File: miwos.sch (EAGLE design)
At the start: 44 parts, among them J1 614004190021, U1 PEC16, U3 PEC16

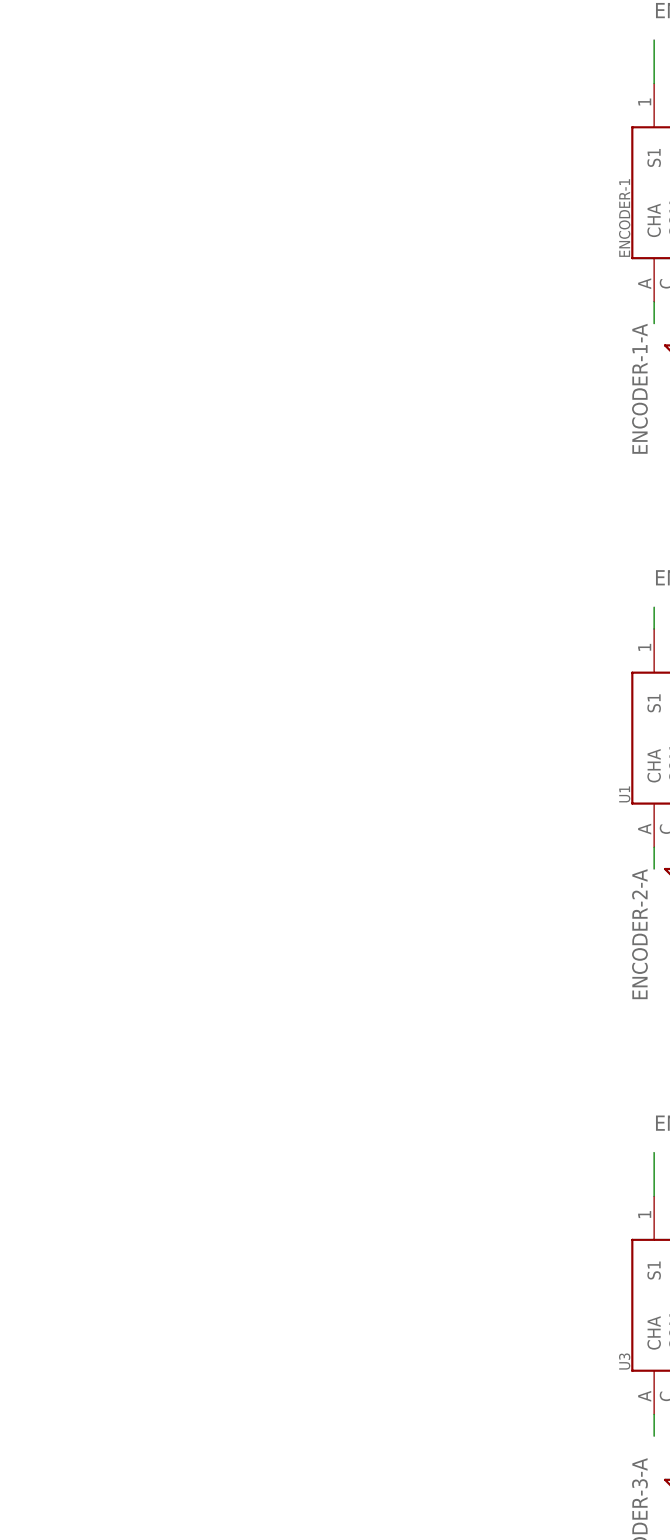
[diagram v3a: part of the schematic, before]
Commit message: Add encoder LEDs, don't wire them for now
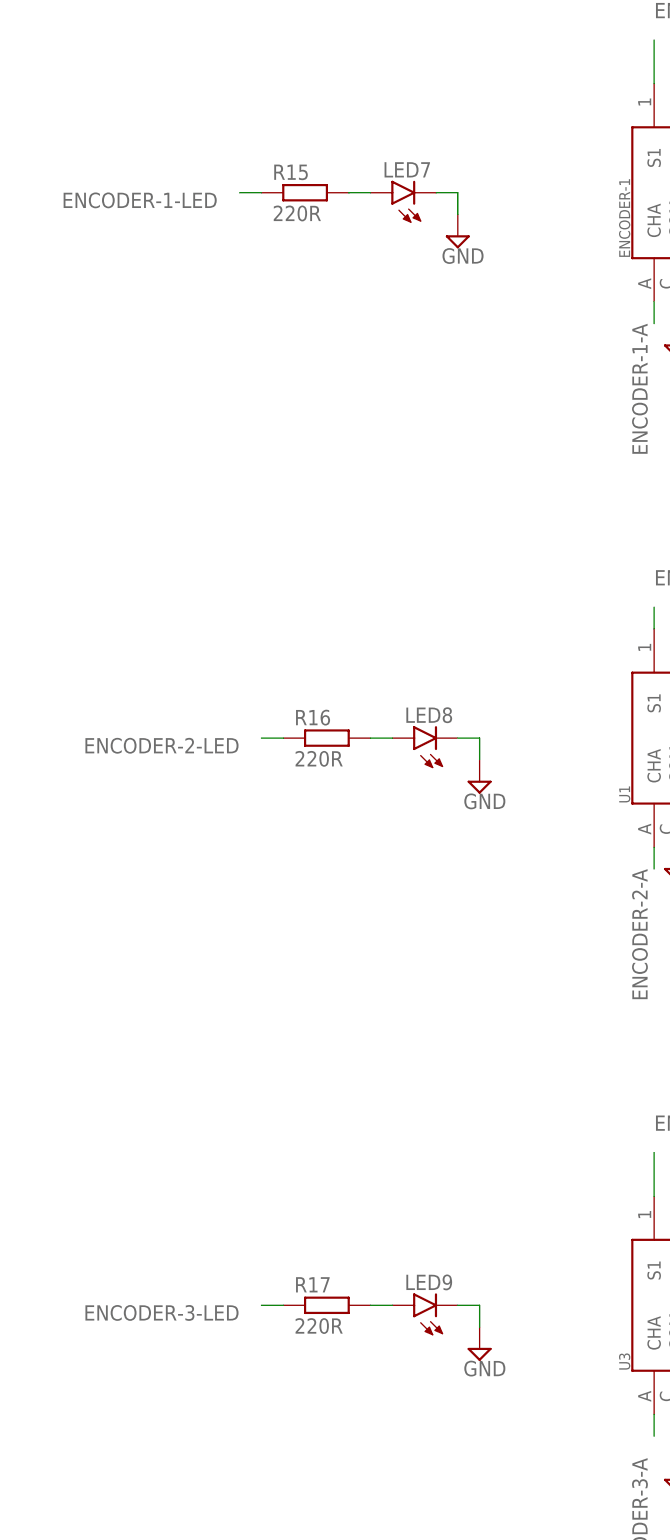
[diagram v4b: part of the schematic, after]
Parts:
- added LED7, LED8, LED9: (no value), led:LED3MM
- added R15, R16, R17: 220R, rcl:R-EU_R0603
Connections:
- new net ENCODER-1-LED: R15.1
- new net ENCODER-2-LED: R16.1
- new net ENCODER-3-LED: R17.1
- new net N$20: LED8.A, R16.2
- new net N$22: LED9.A, R17.2
- new net N$4: LED7.A, R15.2
- net GND: now also LED7.C, LED8.C, LED9.C
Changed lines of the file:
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@@
 <part name="P+4" library="supply1" library_urn="urn:adsk.eagle:library:371" deviceset="+5V" device=""/>
 <part name="SUPPLY29" library="supply2" library_urn="urn:adsk.eagle:library:372" deviceset="GND" device=""/>
+<part name="LED7" library="led" library_urn="urn:adsk.eagle:library:259" deviceset="LED" device="3MM" package3d_urn="urn:adsk.eagle:package:15797/1"/>
+<part name="SUPPLY30" library="supply2" library_urn="urn:adsk.eagle:library:372" deviceset="GND" device=""/>
+<part name="R15" library="rcl" library_urn="urn:adsk.eagle:library:334" deviceset="R-EU_" device="R0603" package3d_urn="urn:adsk.eagle:package:23555/3" value="220R"/>
+<part name="LED8" library="led" library_urn="urn:adsk.eagle:library:259" deviceset="LED" device="3MM" package3d_urn="urn:adsk.eagle:package:15797/1"/>
+<part name="SUPPLY31" library="supply2" library_urn="urn:adsk.eagle:library:372" deviceset="GND" device=""/>
+<part name="R16" library="rcl" library_urn="urn:adsk.eagle:library:334" deviceset="R-EU_" device="R0603" package3d_urn="urn:adsk.eagle:package:23555/3" value="220R"/>
+<part name="LED9" library="led" library_urn="urn:adsk.eagle:library:259" deviceset="LED" device="3MM" package3d_urn="urn:adsk.eagle:package:15797/1"/>
+<part name="SUPPLY32" library="supply2" library_urn="urn:adsk.eagle:library:372" deviceset="GND" device=""/>
+<part name="R17" library="rcl" library_urn="urn:adsk.eagle:library:334" deviceset="R-EU_" device="R0603" package3d_urn="urn:adsk.eagle:package:23555/3" value="220R"/>
 </parts>
 <sheets>
@@
 <instance part="SUPPLY29" gate="GND" x="93.98" y="-5.08" smashed="yes">
 <attribute name="VALUE" x="92.075" y="-8.255" size="1.778" layer="96"/>
+</instance>
+<instance part="LED7" gate="G$1" x="-116.84" y="119.38" smashed="yes" rot="R90">
+<attribute name="NAME" x="-112.268" y="122.936" size="1.778" layer="95" rot="R180"/>
+<attribute name="VALUE" x="-112.268" y="125.095" size="1.778" layer="96" rot="R180"/>
+</instance>
+<instance part="SUPPLY30" gate="GND" x="-109.22" y="114.3" smashed="yes">
+<attribute name="VALUE" x="-111.125" y="111.125" size="1.778" layer="96"/>
+</instance>
+<instance part="R15" gate="G$1" x="-127" y="119.38" smashed="yes">
+<attribute name="NAME" x="-130.81" y="120.8786" size="1.778" layer="95"/>
+<attribute name="VALUE" x="-130.81" y="116.078" size="1.778" layer="96"/>
+</instance>
+<instance part="LED8" gate="G$1" x="-114.3" y="55.88" smashed="yes" rot="R90">
+<attribute name="NAME" x="-109.728" y="59.436" size="1.778" layer="95" rot="R180"/>
+<attribute name="VALUE" x="-109.728" y="61.595" size="1.778" layer="96" rot="R180"/>
+</instance>
+<instance part="SUPPLY31" gate="GND" x="-106.68" y="50.8" smashed="yes">
+<attribute name="VALUE" x="-108.585" y="47.625" size="1.778" layer="96"/>
+</instance>
+<instance part="R16" gate="G$1" x="-124.46" y="55.88" smashed="yes">
+<attribute name="NAME" x="-128.27" y="57.3786" size="1.778" layer="95"/>
+<attribute name="VALUE" x="-128.27" y="52.578" size="1.778" layer="96"/>
+</instance>
+<instance part="LED9" gate="G$1" x="-114.3" y="-10.16" smashed="yes" rot="R90">
+<attribute name="NAME" x="-109.728" y="-6.604" size="1.778" layer="95" rot="R180"/>
+<attribute name="VALUE" x="-109.728" y="-4.445" size="1.778" layer="96" rot="R180"/>
+</instance>
+<instance part="SUPPLY32" gate="GND" x="-106.68" y="-15.24" smashed="yes">
+<attribute name="VALUE" x="-108.585" y="-18.415" size="1.778" layer="96"/>
+</instance>
+<instance part="R17" gate="G$1" x="-124.46" y="-10.16" smashed="yes">
+<attribute name="NAME" x="-128.27" y="-8.6614" size="1.778" layer="95"/>
+<attribute name="VALUE" x="-128.27" y="-13.462" size="1.778" layer="96"/>
 </instance>
 </instances>
@@
 <pinref part="SUPPLY29" gate="GND" pin="GND"/>
 </segment>
+<segment>
+<pinref part="LED7" gate="G$1" pin="C"/>
+<pinref part="SUPPLY30" gate="GND" pin="GND"/>
+<wire x1="-111.76" y1="119.38" x2="-109.22" y2="119.38" width="0.1524" layer="91"/>
+<wire x1="-109.22" y1="119.38" x2="-109.22" y2="116.84" width="0.1524" layer="91"/>
+</segment>
+<segment>
+<pinref part="LED8" gate="G$1" pin="C"/>
+<pinref part="SUPPLY31" gate="GND" pin="GND"/>
+<wire x1="-109.22" y1="55.88" x2="-106.68" y2="55.88" width="0.1524" layer="91"/>
+<wire x1="-106.68" y1="55.88" x2="-106.68" y2="53.34" width="0.1524" layer="91"/>
+</segment>
+<segment>
+<pinref part="LED9" gate="G$1" pin="C"/>
+<pinref part="SUPPLY32" gate="GND" pin="GND"/>
+<wire x1="-109.22" y1="-10.16" x2="-106.68" y2="-10.16" width="0.1524" layer="91"/>
+<wire x1="-106.68" y1="-10.16" x2="-106.68" y2="-12.7" width="0.1524" layer="91"/>
+</segment>
 </net>
 <net name="ENCODER-2-A" class="0">
@@
 </segment>
 </net>
+<net name="N$4" class="0">
+<segment>
+<pinref part="LED7" gate="G$1" pin="A"/>
+<wire x1="-119.38" y1="119.38" x2="-121.92" y2="119.38" width="0.1524" layer="91"/>
+<pinref part="R15" gate="G$1" pin="2"/>
+</segment>
+</net>
+<net name="N$20" class="0">
+<segment>
+<pinref part="LED8" gate="G$1" pin="A"/>
+<wire x1="-116.84" y1="55.88" x2="-119.38" y2="55.88" width="0.1524" layer="91"/>
+<pinref part="R16" gate="G$1" pin="2"/>
+</segment>
+</net>
+<net name="N$22" class="0">
+<segment>
+<pinref part="LED9" gate="G$1" pin="A"/>
+<wire x1="-116.84" y1="-10.16" x2="-119.38" y2="-10.16" width="0.1524" layer="91"/>
+<pinref part="R17" gate="G$1" pin="2"/>
+</segment>
+</net>
+<net name="ENCODER-1-LED" class="0">
+<segment>
+<label x="-137.16" y="119.38" size="1.778" layer="95" rot="R180"/>
+<wire x1="-132.08" y1="119.38" x2="-134.62" y2="119.38" width="0.1524" layer="91"/>
+<pinref part="R15" gate="G$1" pin="1"/>
+</segment>
+</net>
+<net name="ENCODER-2-LED" class="0">
+<segment>
+<label x="-134.62" y="55.88" size="1.778" layer="95" rot="R180"/>
+<wire x1="-129.54" y1="55.88" x2="-132.08" y2="55.88" width="0.1524" layer="91"/>
+<pinref part="R16" gate="G$1" pin="1"/>
+</segment>
+</net>
+<net name="ENCODER-3-LED" class="0">
+<segment>
+<label x="-134.62" y="-10.16" size="1.778" layer="95" rot="R180"/>
+<wire x1="-129.54" y1="-10.16" x2="-132.08" y2="-10.16" width="0.1524" layer="91"/>
+<pinref part="R17" gate="G$1" pin="1"/>
+</segment>
+</net>

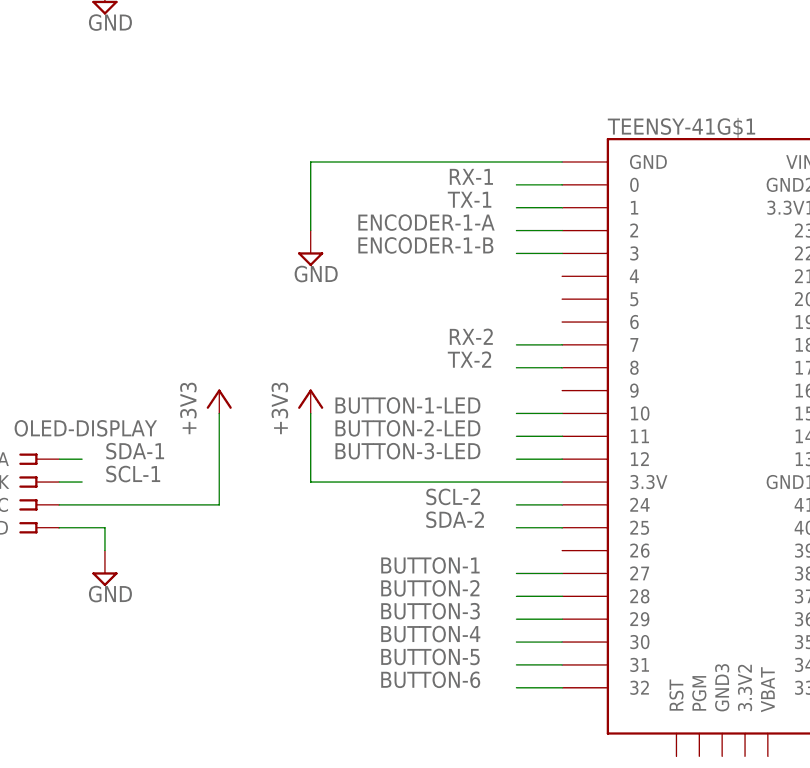
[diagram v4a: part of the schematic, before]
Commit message: Wire encoder LEDs
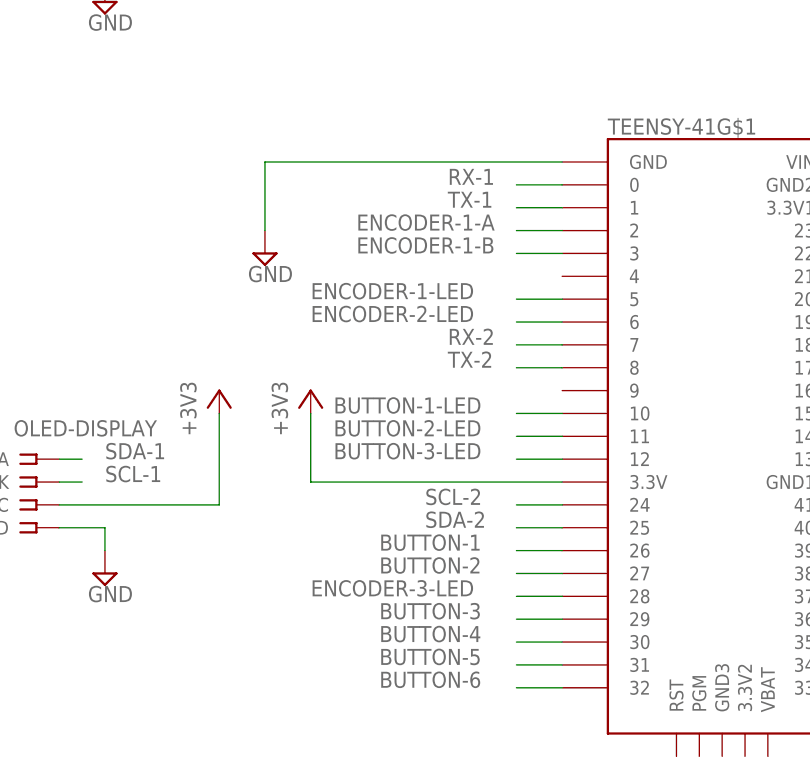
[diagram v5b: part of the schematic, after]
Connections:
- net BUTTON-1: now also TEENSY-41G$1.26; no longer TEENSY-41G$1.27
- net BUTTON-2: now also TEENSY-41G$1.27; no longer TEENSY-41G$1.28
- net ENCODER-1-LED: now also TEENSY-41G$1.5
- net ENCODER-2-LED: now also TEENSY-41G$1.6
- net ENCODER-3-LED: now also TEENSY-41G$1.28
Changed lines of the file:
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@@
 <attribute name="VALUE" x="53.34" y="99.06" size="1.778" layer="96" rot="R90"/>
 </instance>
-<instance part="SUPPLY9" gate="GND" x="-20.32" y="81.28" smashed="yes">
-<attribute name="VALUE" x="-22.225" y="78.105" size="1.778" layer="96"/>
+<instance part="SUPPLY9" gate="GND" x="-25.4" y="81.28" smashed="yes">
+<attribute name="VALUE" x="-27.305" y="78.105" size="1.778" layer="96"/>
 </instance>
 <instance part="R3" gate="G$1" x="121.92" y="137.16" smashed="yes">
@@
 <segment>
 <pinref part="SUPPLY9" gate="GND" pin="GND"/>
-<wire x1="-20.32" y1="83.82" x2="-20.32" y2="91.44" width="0.1524" layer="91"/>
+<wire x1="-25.4" y1="83.82" x2="-25.4" y2="91.44" width="0.1524" layer="91"/>
 <pinref part="TEENSY-41" gate="G$1" pin="GND"/>
-<wire x1="-20.32" y1="91.44" x2="7.62" y2="91.44" width="0.1524" layer="91"/>
+<wire x1="-25.4" y1="91.44" x2="7.62" y2="91.44" width="0.1524" layer="91"/>
 </segment>
 <segment>
@@
 </segment>
 <segment>
+<pinref part="TEENSY-41" gate="G$1" pin="26"/>
+<wire x1="7.62" y1="48.26" x2="2.54" y2="48.26" width="0.1524" layer="91"/>
+<label x="-12.7" y="48.26" size="1.778" layer="95"/>
+</segment>
+</net>
+<net name="BUTTON-2" class="0">
+<segment>
+<pinref part="S2" gate="G$1" pin="COM"/>
+<wire x1="33.02" y1="-43.18" x2="30.48" y2="-43.18" width="0.1524" layer="91"/>
+<label x="27.94" y="-43.18" size="1.778" layer="95" rot="R180"/>
+</segment>
+<segment>
 <pinref part="TEENSY-41" gate="G$1" pin="27"/>
 <wire x1="7.62" y1="45.72" x2="2.54" y2="45.72" width="0.1524" layer="91"/>
 <label x="-12.7" y="45.72" size="1.778" layer="95"/>
-</segment>
-</net>
-<net name="BUTTON-2" class="0">
-<segment>
-<pinref part="S2" gate="G$1" pin="COM"/>
-<wire x1="33.02" y1="-43.18" x2="30.48" y2="-43.18" width="0.1524" layer="91"/>
-<label x="27.94" y="-43.18" size="1.778" layer="95" rot="R180"/>
-</segment>
-<segment>
-<pinref part="TEENSY-41" gate="G$1" pin="28"/>
-<wire x1="7.62" y1="43.18" x2="2.54" y2="43.18" width="0.1524" layer="91"/>
-<label x="-12.7" y="43.18" size="1.778" layer="95"/>
 </segment>
 </net>
@@
 <pinref part="R15" gate="G$1" pin="1"/>
 </segment>
+<segment>
+<pinref part="TEENSY-41" gate="G$1" pin="5"/>
+<wire x1="7.62" y1="76.2" x2="2.54" y2="76.2" width="0.1524" layer="91"/>
+<label x="-20.32" y="76.2" size="1.778" layer="95"/>
+</segment>
 </net>
 <net name="ENCODER-2-LED" class="0">
@@
 <pinref part="R16" gate="G$1" pin="1"/>
 </segment>
+<segment>
+<pinref part="TEENSY-41" gate="G$1" pin="6"/>
+<wire x1="7.62" y1="73.66" x2="2.54" y2="73.66" width="0.1524" layer="91"/>
+<label x="-20.32" y="73.66" size="1.778" layer="95"/>
+</segment>
 </net>
 <net name="ENCODER-3-LED" class="0">
@@
 <pinref part="R17" gate="G$1" pin="1"/>
 </segment>
-</net>
+<segment>
+<pinref part="TEENSY-41" gate="G$1" pin="28"/>
+<wire x1="7.62" y1="43.18" x2="2.54" y2="43.18" width="0.1524" layer="91"/>
+<label x="-20.32" y="43.18" size="1.778" layer="95"/>
+</segment>
+</net>

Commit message: Place labels, small fixes
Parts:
- removed MIDI-IN-1, MIDI-IN-2, MIDI-OUT-1, MIDI-OUT-2: ADAFRUIT-5PIN-DIN, adafruit-5pin-din:ADAFRUIT-5PIN-DIN
- added MIDI1-IN, MIDI1-OUT, MIDI2-IN, MIDI2-OUT: ADAFRUIT-5PIN-DIN, adafruit-5pin-din:ADAFRUIT-5PIN-DIN
- renumbered DISPLAY to DISPLAY1, DISPLAY-1 to DISPLAY2, DISPLAY-2 to DISPLAY3, ENCODER-1 to ENCODER1, J1 to USB-HUB, S1 to BUTTON1, S2 to BUTTON2, S3 to BUTTON3, S4 to BUTTON4, S5 to BUTTON5, S6 to BUTTON6, U1 to ENCODER2, U3 to ENCODER3
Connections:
- net BUTTON-1 renamed BUTTON1
- net BUTTON-1-LED renamed BUTTON1-LED
- net BUTTON-2 renamed BUTTON2
- net BUTTON-2-LED renamed BUTTON2-LED
- net BUTTON-3 renamed BUTTON3
- net BUTTON-3-LED renamed BUTTON3-LED
- net BUTTON-4 renamed BUTTON4
- net BUTTON-4-LED renamed BUTTON4-LED
- net BUTTON-5 renamed BUTTON5
- net BUTTON-5-LED renamed BUTTON5-LED
- net BUTTON-6 renamed BUTTON6
- net BUTTON-6-LED renamed BUTTON6-LED
- net ENCODER-1-A renamed ENCODER1-A
- net ENCODER-1-B renamed ENCODER1-B
- net ENCODER-1-LED renamed ENCODER1-LED
- net ENCODER-1-PUSH renamed ENCODER1-PUSH
- net ENCODER-2-A renamed ENCODER2-A
- net ENCODER-2-B renamed ENCODER2-B
- net ENCODER-2-LED renamed ENCODER2-LED
- net ENCODER-2-PUSH renamed ENCODER2-PUSH
- net ENCODER-3-A renamed ENCODER3-A
- net ENCODER-3-B renamed ENCODER3-B
- net ENCODER-3-LED renamed ENCODER3-LED
- net ENCODER-3-PUSH renamed ENCODER3-PUSH
- net RX-1 renamed RX1
- net RX-2 renamed RX2
- net RX-5 renamed RX5
- net SCL-1 renamed SCL1
- net SCL-2 renamed SCL2
- net SDA-1 renamed SDA1
- net SDA-2 renamed SDA2
- net TX-1 renamed TX1
- net TX-2 renamed TX2
- net TX-5 renamed TX5
- net GND: now also MIDI1-OUT.2, MIDI2-OUT.2; no longer MIDI-OUT-1.2, MIDI-OUT-2.2
- net N$10: now also MIDI1-IN.4; no longer MIDI-IN-2.4
- net N$11: now also MIDI1-OUT.5; no longer MIDI-OUT-2.5
- net N$12: now also MIDI1-OUT.4; no longer MIDI-OUT-2.4
- net N$17: now also MIDI2-IN.5; no longer MIDI-IN-1.5
- net N$18: now also MIDI2-IN.4; no longer MIDI-IN-1.4
- net N$19: now also MIDI2-OUT.5; no longer MIDI-OUT-1.5
- net N$21: now also MIDI2-OUT.4; no longer MIDI-OUT-1.4
- net N$9: now also MIDI1-IN.5; no longer MIDI-IN-2.5
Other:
- moved on the sheet: C1, C2, D1, D2, OK1, OK2, R1, R10, R11, R2, R3, R4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
